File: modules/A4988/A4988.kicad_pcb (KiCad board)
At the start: 2 copper layers, 40.6 x 40.6 mm, 15 parts, among them J1 Conn_01x10_Male, J2 Conn_01x10_Male, J3 Conn_01x08_Female, J4 Conn_01x08_Female, J5 Conn_01x04_Male, J6 Conn_01x02_Female, SW1 SW_DIP_x03

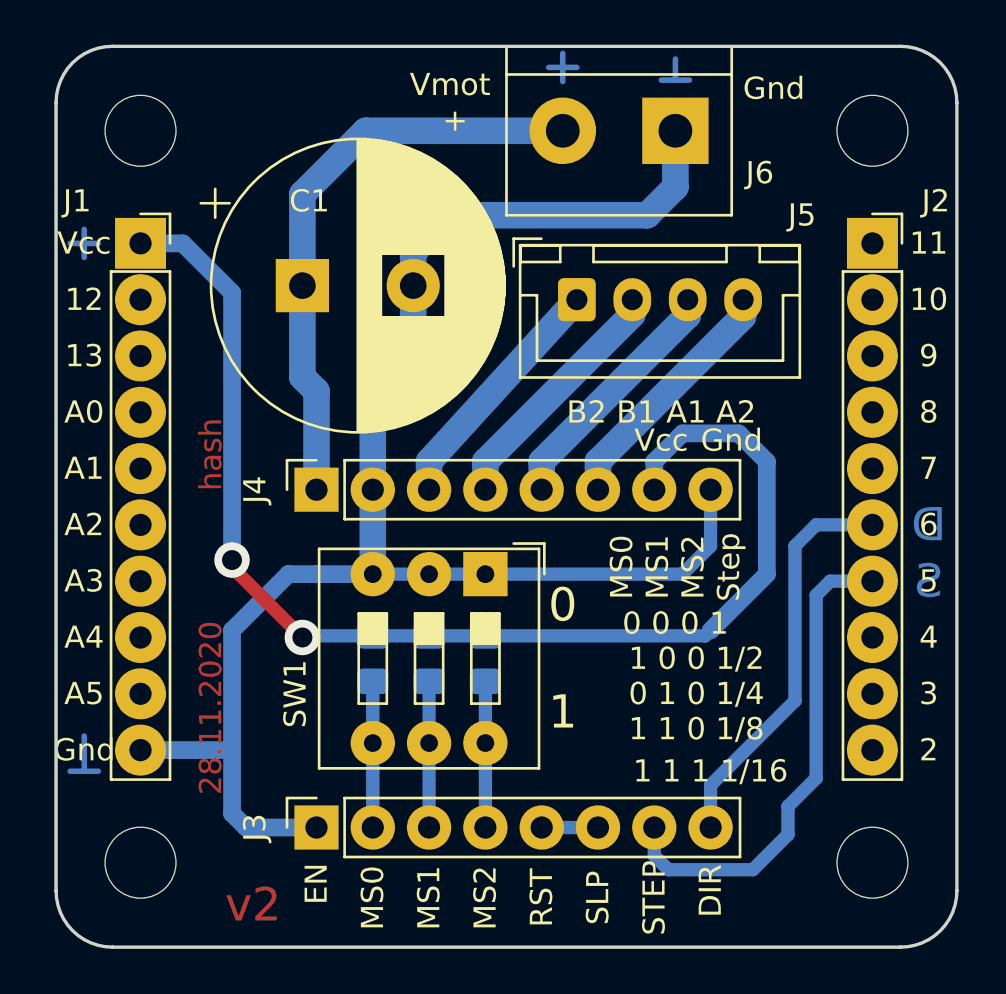
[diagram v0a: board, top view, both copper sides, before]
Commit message: A4988. Fix hash, add gerber.
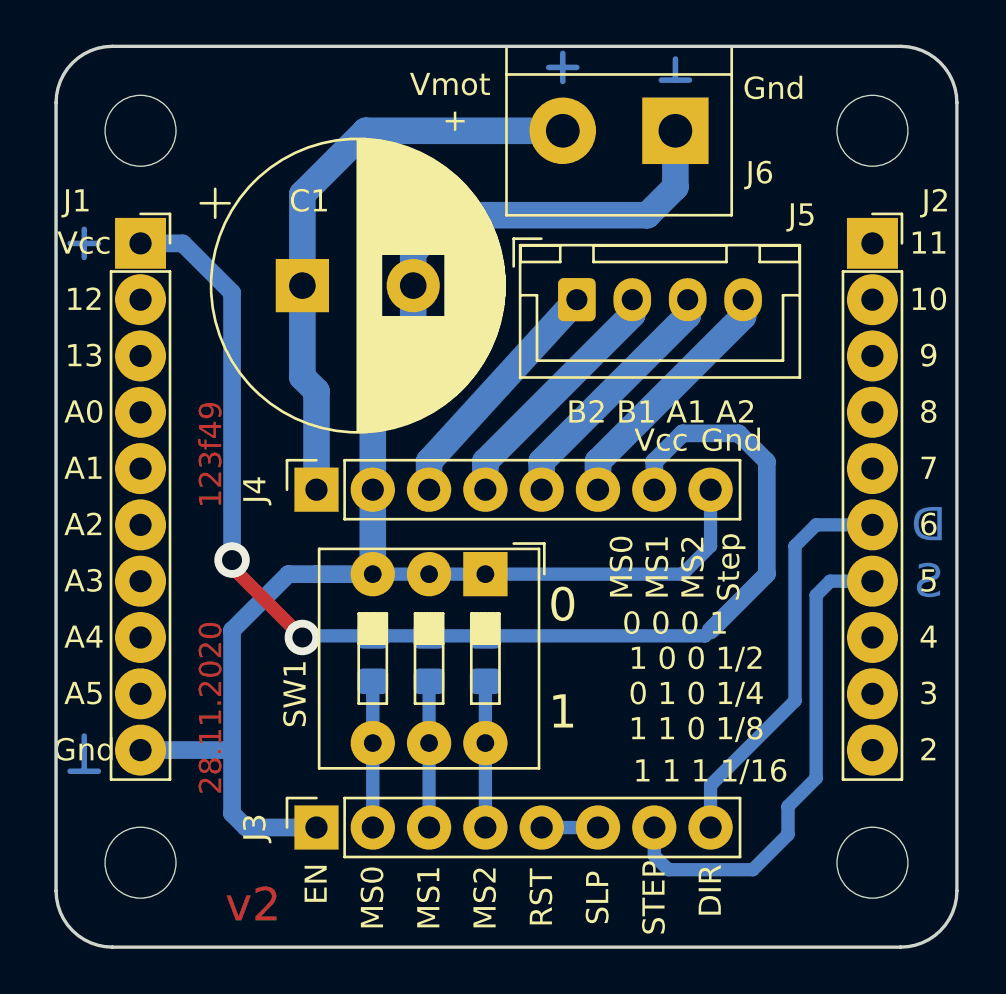
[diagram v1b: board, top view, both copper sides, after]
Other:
- board text added: "123f49"
- board text removed: "hash"
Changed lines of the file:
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@@
     (visible_elements 7FFFFFFF)
     (pcbplotparams
-      (layerselection 0x010fc_ffffffff)
+      (layerselection 0x010f0_ffffffff)
       (usegerberextensions false)
       (usegerberattributes false)
@@
       (outputformat 1)
       (mirror false)
-      (drillshape 1)
+      (drillshape 0)
       (scaleselection 1)
-      (outputdirectory ""))
+      (outputdirectory "gerber/"))
   )
   (net 0 "")
@@
       (effects (font (size 1 1) (thickness 0.15)))
     )
-    (pad 1 thru_hole roundrect (at 0 0) (size 1.7 1.95) (drill 0.95) (layers *.Cu *.Mask) (roundrect_rratio 0.147059)
+    (pad 1 thru_hole roundrect (at 0 0) (size 1.7 1.95) (drill 0.95) (layers *.Cu *.Mask) (roundrect_rratio 0.1470588235294118)
       (net 29 /MB2))
     (pad 2 thru_hole oval (at 2.5 0) (size 1.7 1.95) (drill 0.95) (layers *.Cu *.Mask)
@@
       (effects (font (size 0.5 0.5) (thickness 0.08)) (justify mirror))
     )
-    (pad 1 smd roundrect (at -1.025 0 270) (size 1.15 1.4) (layers B.Cu B.Paste B.Mask) (roundrect_rratio 0.217391)
+    (pad 1 smd roundrect (at -1.025 0 270) (size 1.15 1.4) (layers B.Cu B.Paste B.Mask) (roundrect_rratio 0.2173904347826087)
       (net 1 VCC))
-    (pad 2 smd roundrect (at 1.025 0 270) (size 1.15 1.4) (layers B.Cu B.Paste B.Mask) (roundrect_rratio 0.217391)
+    (pad 2 smd roundrect (at 1.025 0 270) (size 1.15 1.4) (layers B.Cu B.Paste B.Mask) (roundrect_rratio 0.2173904347826087)
       (net 22 /MS0))
     (model ${KISYS3DMOD}/Resistor_SMD.3dshapes/R_0805_2012Metric.wrl
@@
       (effects (font (size 0.5 0.5) (thickness 0.08)) (justify mirror))
     )
-    (pad 2 smd roundrect (at 1.025 0 270) (size 1.15 1.4) (layers B.Cu B.Paste B.Mask) (roundrect_rratio 0.217391)
+    (pad 2 smd roundrect (at 1.025 0 270) (size 1.15 1.4) (layers B.Cu B.Paste B.Mask) (roundrect_rratio 0.2173904347826087)
       (net 23 /MS1))
-    (pad 1 smd roundrect (at -1.025 0 270) (size 1.15 1.4) (layers B.Cu B.Paste B.Mask) (roundrect_rratio 0.217391)
+    (pad 1 smd roundrect (at -1.025 0 270) (size 1.15 1.4) (layers B.Cu B.Paste B.Mask) (roundrect_rratio 0.2173904347826087)
       (net 1 VCC))
     (model ${KISYS3DMOD}/Resistor_SMD.3dshapes/R_0805_2012Metric.wrl
@@
       (effects (font (size 0.5 0.5) (thickness 0.08)) (justify mirror))
     )
-    (pad 1 smd roundrect (at -1.025 0 270) (size 1.15 1.4) (layers B.Cu B.Paste B.Mask) (roundrect_rratio 0.217391)
+    (pad 1 smd roundrect (at -1.025 0 270) (size 1.15 1.4) (layers B.Cu B.Paste B.Mask) (roundrect_rratio 0.2173904347826087)
       (net 1 VCC))
-    (pad 2 smd roundrect (at 1.025 0 270) (size 1.15 1.4) (layers B.Cu B.Paste B.Mask) (roundrect_rratio 0.217391)
+    (pad 2 smd roundrect (at 1.025 0 270) (size 1.15 1.4) (layers B.Cu B.Paste B.Mask) (roundrect_rratio 0.2173904347826087)
       (net 24 /MS2))
     (model ${KISYS3DMOD}/Resistor_SMD.3dshapes/R_0805_2012Metric.wrl
@@
     (effects (font (size 1 1) (thickness 0.15)))
   )
-  (gr_text hash (at 95.885 69.215 90) (layer F.Cu)
+  (gr_text 123f49 (at 95.885 69.215 90) (layer F.Cu)
     (effects (font (size 1 1) (thickness 0.2)))
   )

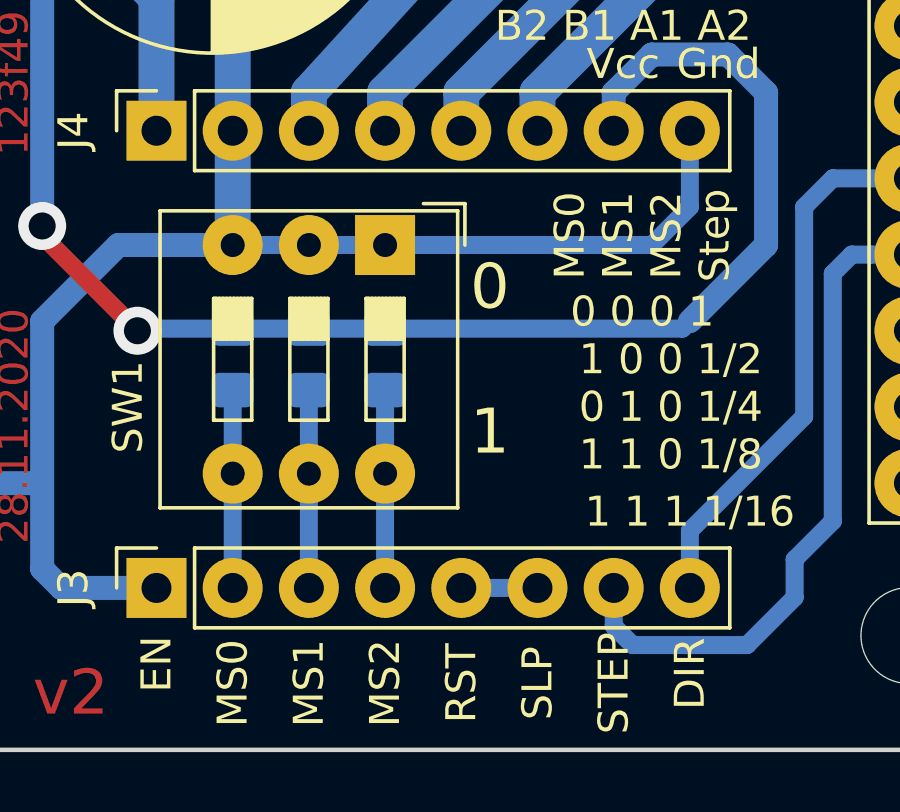
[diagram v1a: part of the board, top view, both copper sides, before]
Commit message: A4988. Fix pin names
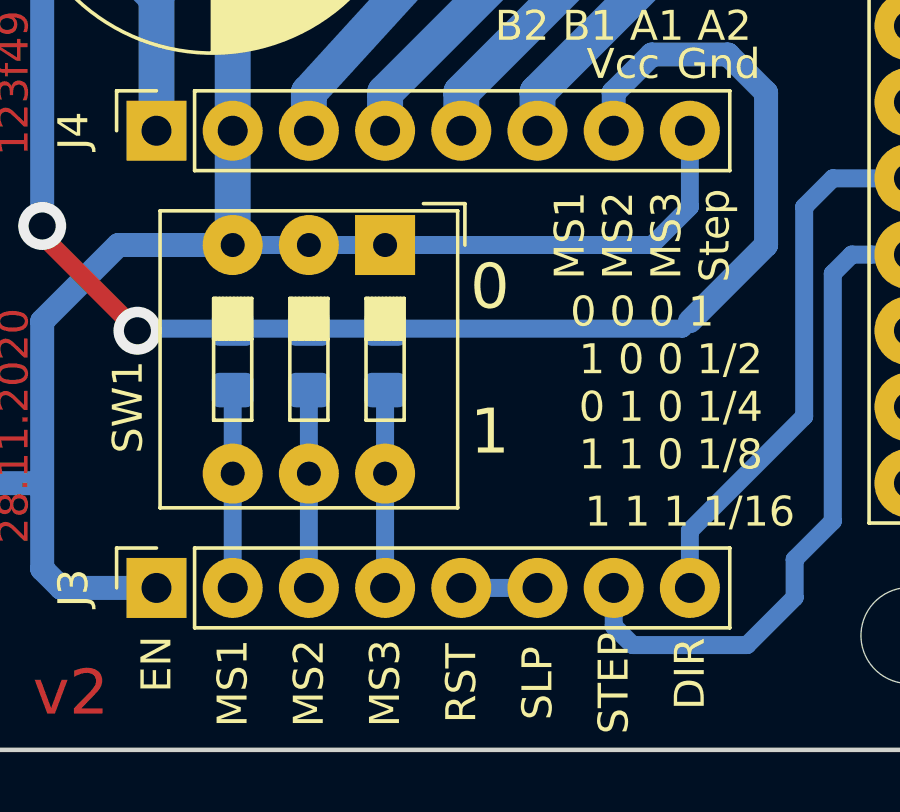
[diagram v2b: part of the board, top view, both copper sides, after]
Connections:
- J3 pad 2: /MS0 -> /MS1
- J3 pad 3: /MS1 -> /MS2
- J3 pad 4: /MS2 -> /MS3
- R1 pad 2: /MS0 -> /MS1
- R2 pad 2: /MS1 -> /MS2
- R3 pad 2: /MS2 -> /MS3
- SW1 pad 4: /MS0 -> /MS1
- SW1 pad 5: /MS1 -> /MS2
- SW1 pad 6: /MS2 -> /MS3
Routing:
- net /MS3: track 0.00 -> 6.59 mm
- net /MS0: track 6.59 -> 0.00 mm
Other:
- board text added: "MS1 MS2 MS3 Step"
- board text added: "MS3"
- board text removed: "MS0"
- board text removed: "MS0 MS1 MS2 Step"

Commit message: Fix hash, fix gerber
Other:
- board text added: "bb56cf"
- board text removed: "123f49"

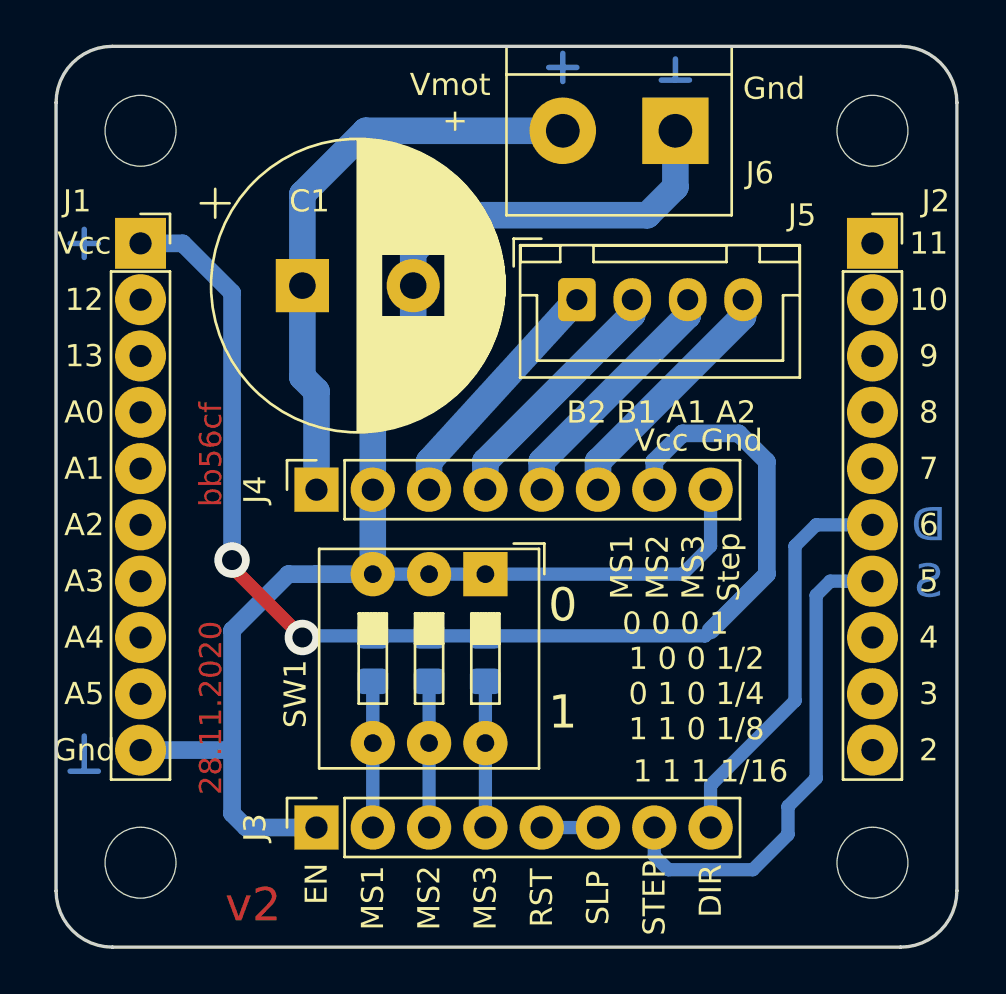
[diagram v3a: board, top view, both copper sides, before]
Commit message: 1x PCBs. Move holes to edges. Caution! This changes is uncompatible with previous versions...
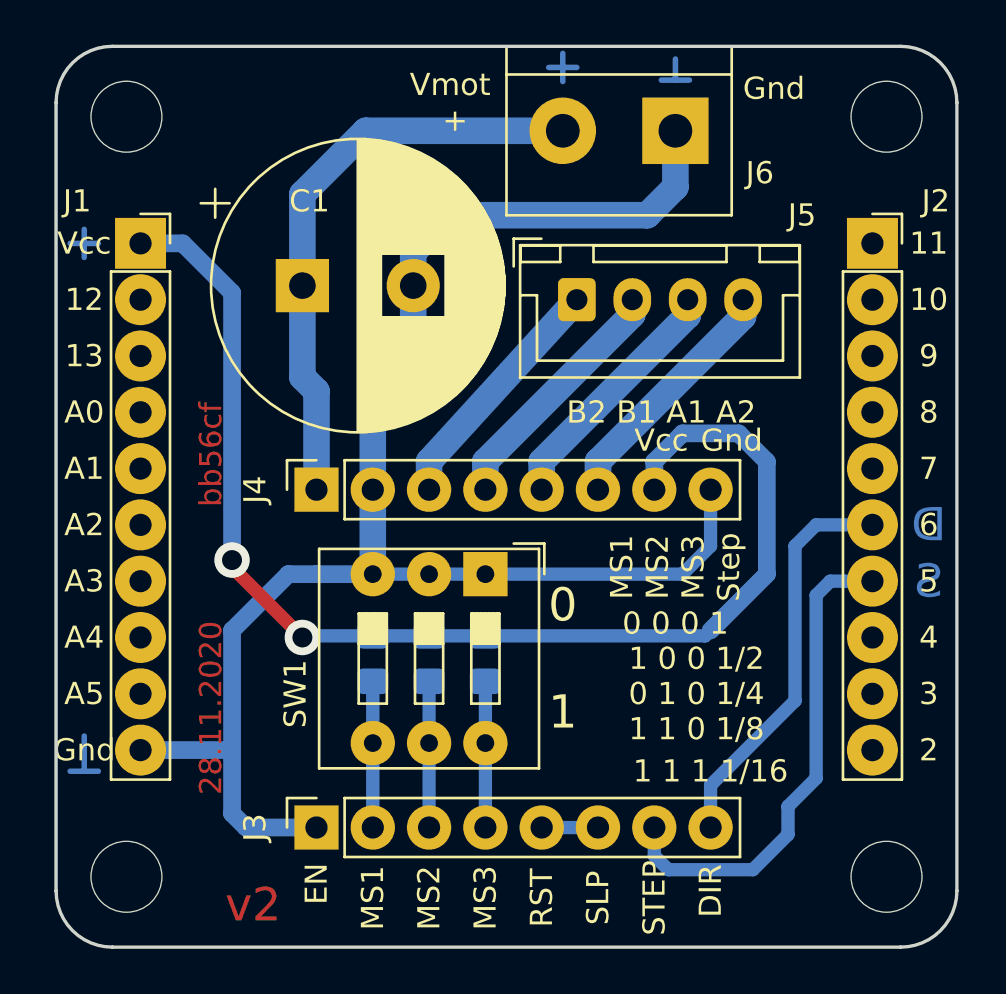
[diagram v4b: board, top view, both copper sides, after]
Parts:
- moved H2 0.90 mm to (92.1, 88.3)
- moved H4 0.90 mm to (126.4, 88.3)
- moved H1 0.90 mm to (92.1, 54.0)
- moved H3 0.90 mm to (126.4, 54.0)
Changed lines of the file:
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@@
   )
   (module MountingHole:MountingHole_3.2mm_M3 (layer F.Cu)
-    (at 92.71 54.61)
+    (at 92.0750 53.9750)
     (descr "Mounting Hole 3.2mm, no annular, M3")
     (tags "mounting hole 3.2mm no annular m3")
@@
   )
   (module MountingHole:MountingHole_3.2mm_M3 (layer F.Cu)
-    (at 92.71 87.63)
+    (at 92.0750 88.2650)
     (descr "Mounting Hole 3.2mm, no annular, M3")
     (tags "mounting hole 3.2mm no annular m3")
@@
   )
   (module MountingHole:MountingHole_3.2mm_M3 (layer F.Cu)
-    (at 125.73 54.61)
+    (at 126.3650 53.9750)
     (descr "Mounting Hole 3.2mm, no annular, M3")
     (tags "mounting hole 3.2mm no annular m3")
@@
   )
   (module MountingHole:MountingHole_3.2mm_M3 (layer F.Cu)
-    (at 125.73 87.63)
+    (at 126.3650 88.2650)
     (descr "Mounting Hole 3.2mm, no annular, M3")
     (tags "mounting hole 3.2mm no annular m3")

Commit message: A4988. Add jumpers & pull-ups, FIX SOCKET!, polishing
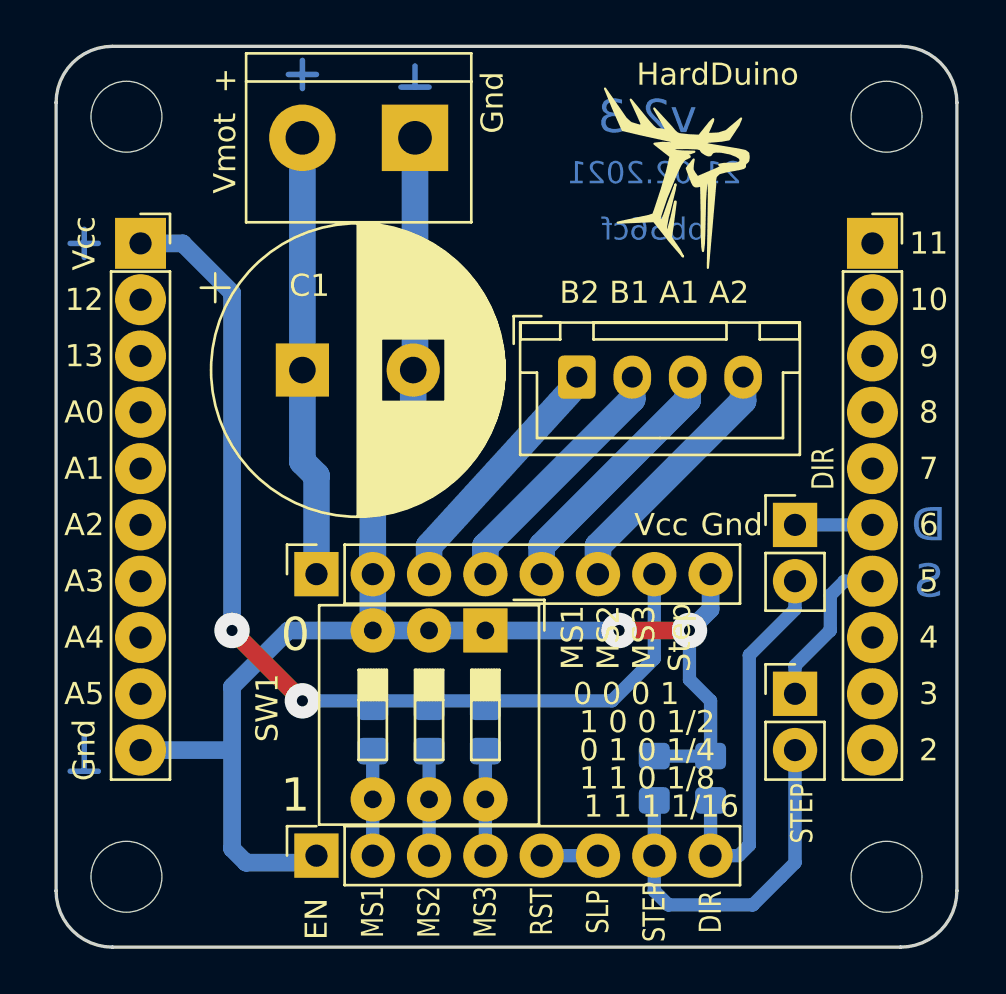
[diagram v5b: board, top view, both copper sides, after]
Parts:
- added JP1: Jumper, Connector_PinHeader_2.54mm:PinHeader_1x02_P2.54mm_Vertical, F.Cu at (122.2, 80.0)
- added JP2: Jumper, Connector_PinHeader_2.54mm:PinHeader_1x02_P2.54mm_Vertical, F.Cu at (122.2, 72.4)
- added R4: 10k, Resistor_SMD:R_0805_2012Metric_Pad1.20x1.40mm_HandSolder, B.Cu at (115.9, 83.8)
- added R5: 10k, Resistor_SMD:R_0805_2012Metric_Pad1.20x1.40mm_HandSolder, B.Cu at (118.4, 83.8)
- R1, R2, R3: footprint Resistor_SMD:R_0805_2012Metric_Pad1.15x1.40mm_HandSolder -> Resistor_SMD:R_0805_2012Metric_Pad1.20x1.40mm_HandSolder
- moved J6 11.8 mm to (105.1, 54.9)
- moved C1 3.81 mm to (100.0, 65.4)
- moved J4 3.81 mm to (100.6, 74.6)
- moved J5 3.49 mm to (112.4, 65.7)
- moved R1 3.17 mm to (103.2, 81.6)
- moved R2 3.17 mm to (105.7, 81.6)
- moved R3 3.17 mm to (108.3, 81.6)
- moved SW1 2.54 mm to (108.3, 77.2)
- moved J3 1.27 mm to (100.6, 87.3)
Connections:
- J3 pad 7: /5 -> /STEP
- J3 pad 8: /6 -> /DIR
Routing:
- net /DIR: track 0.00 -> 17.2 mm
- net /STEP: track 0.00 -> 16.2 mm
- net /5: track 22.3 -> 7.27 mm
- net /6: track 18.2 -> 3.49 mm
- net VCC: track 56.2 -> 45.2 mm
- net /VMOT: track 26.2 -> 19.6 mm
- net /MS3: track 6.59 -> 5.01 mm
- net /MS2: track 6.59 -> 5.01 mm
- net /MS1: track 6.59 -> 5.01 mm
- net GND: vias 0 -> 2
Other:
- board text added: "21.02.2021"
- board text added: "v2.3"
- board text removed: "28.11.2020"
- board text removed: "v2"

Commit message: Fix hash & version
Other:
- board text added: "b4d799"
- board text removed: "bb56cf"
